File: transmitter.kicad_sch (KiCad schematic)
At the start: 0 parts

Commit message: Polished IO schematics
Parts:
- added U37: STM32H723ZGTx, Package_QFP:LQFP-144_20x20mm_P0.5mm, symbol MCU_ST_STM32H7:STM32H723ZGTx
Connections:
- new net: U37.107 (VSS), U37.120 (VSS), U37.130 (VSS), U37.16 (VSS), U37.38 (VSS), U37.51 (VSS), U37.61 (VSS), U37.83 (VSS), U37.94 (VSS)
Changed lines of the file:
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@@
 (kicad_sch (version 20230121) (generator eeschema)
-  (paper "A4")
-)
+  (paper "A4" portrait)

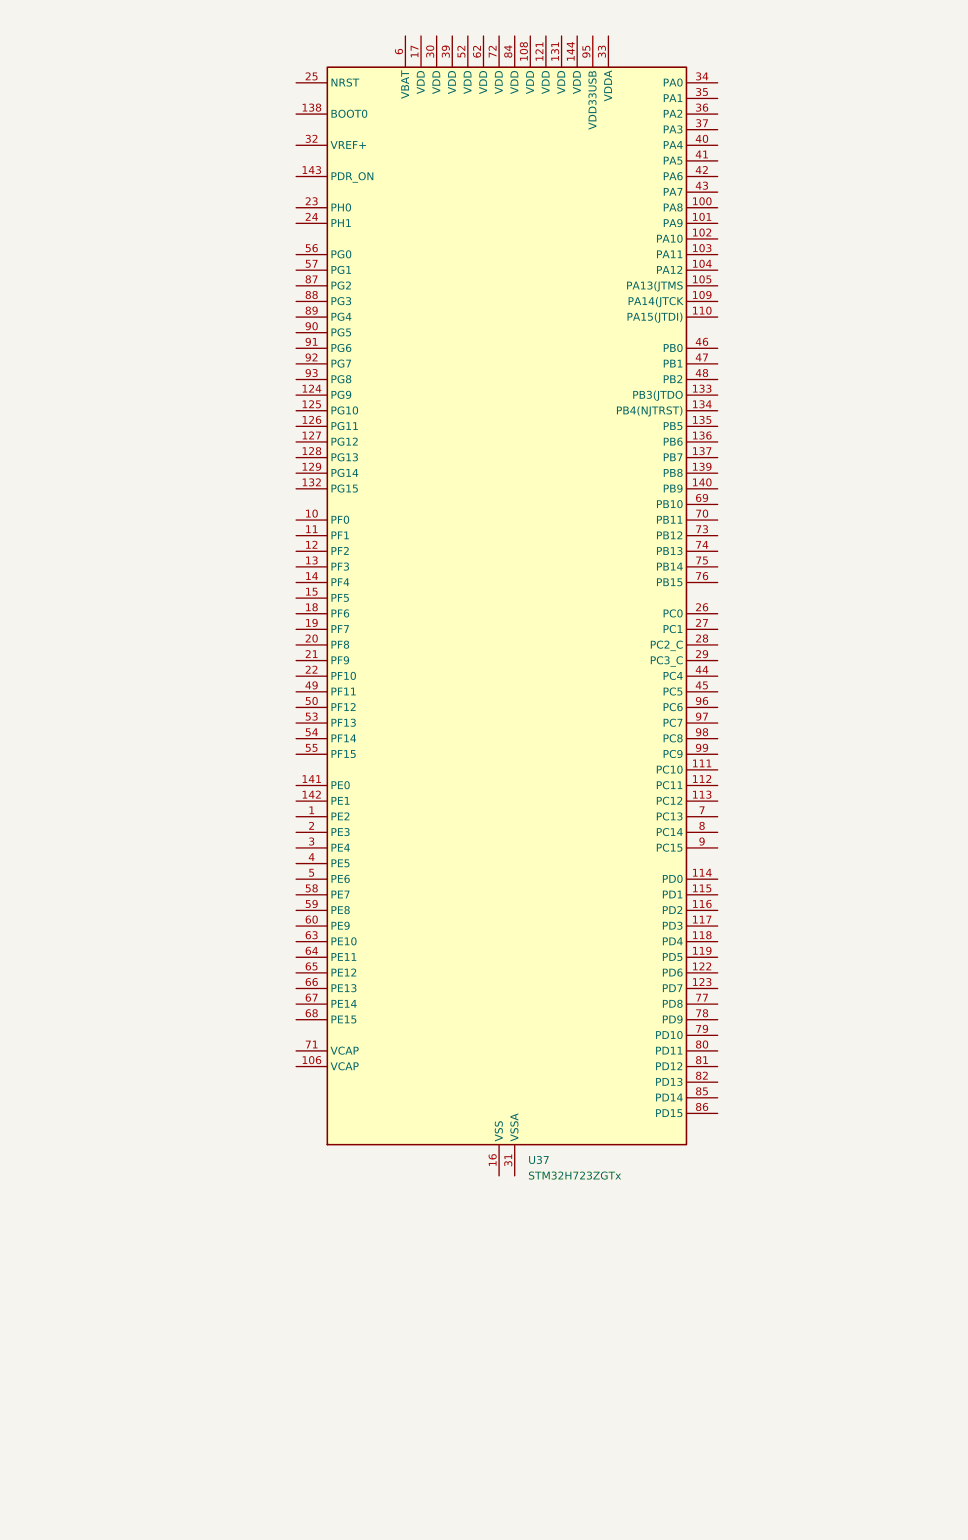
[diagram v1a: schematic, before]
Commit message: Set power routing for stm32
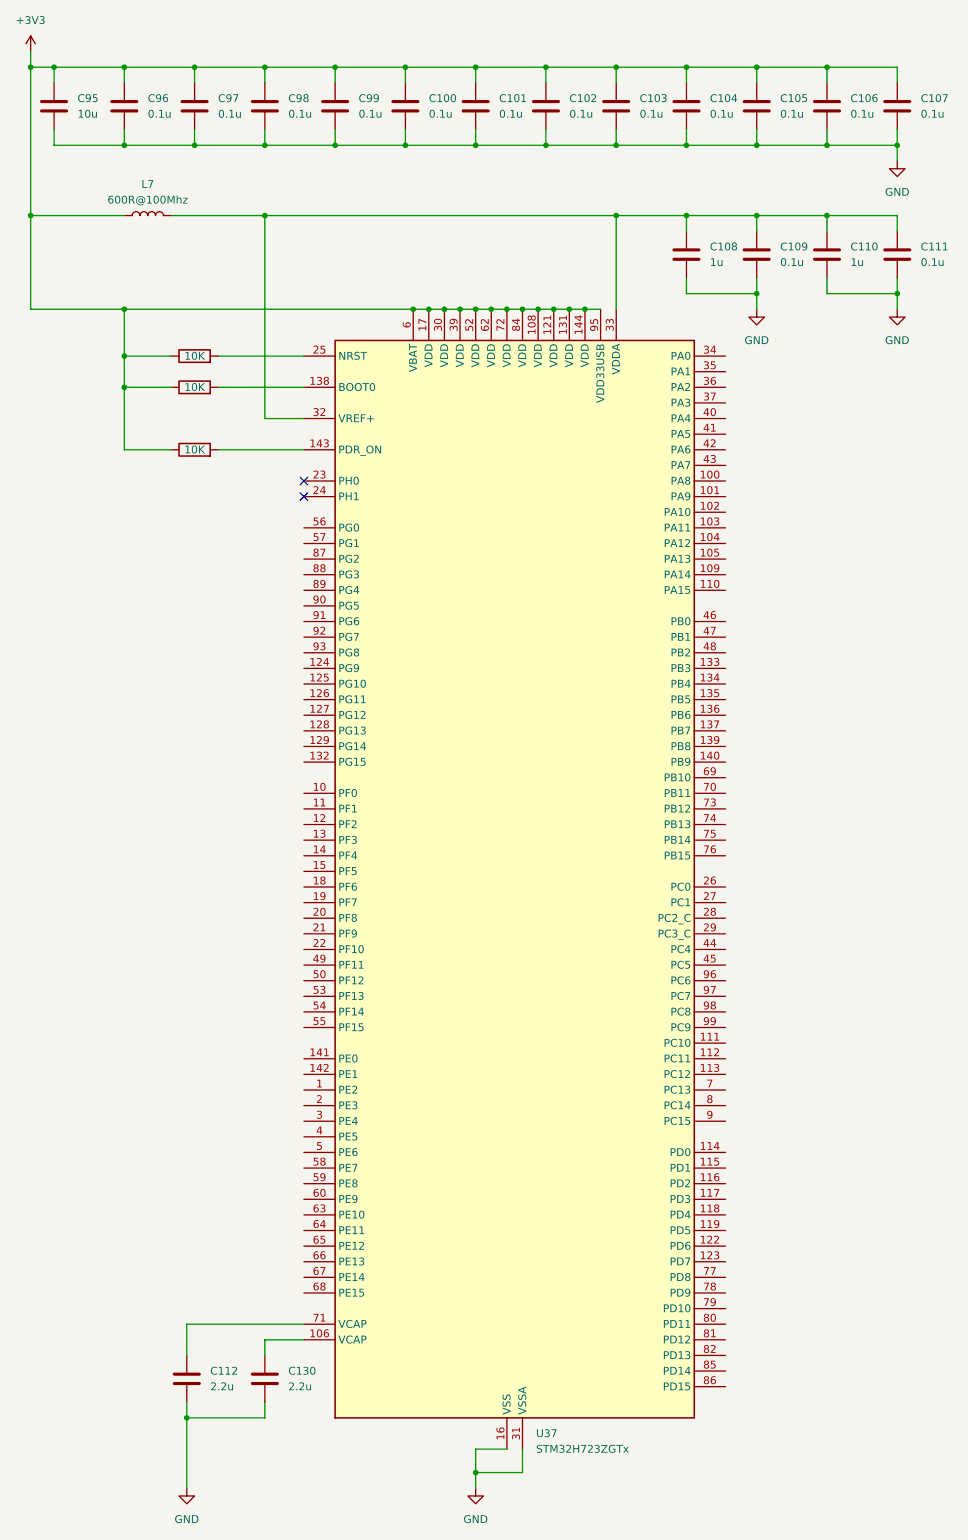
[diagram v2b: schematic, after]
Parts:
- added C100, C101, C102, C103, C104, C105, C106, C107, C109, C111, C96, C97, C98, C99: 0.1u, symbol Device:C
- added C108, C110: 1u, symbol Device:C
- added C112, C130: 2.2u, symbol Device:C
- added C95: 10u, symbol Device:C
- added L7: 600R@100Mhz, symbol Device:L
- added R187, R188, R189: 10K, symbol Device:R
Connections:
- net at U37.106 (VCAP): now also C130.1
- net GND: now reaches U37.107 (VSS), U37.120 (VSS), U37.130 (VSS), U37.16 (VSS), U37.38 (VSS), U37.51 (VSS), U37.61 (VSS), U37.83 (VSS), U37.94 (VSS)
- net GND: now also U37.31 (VSSA), C100.2, C101.2, C102.2, C103.2, C104.2, C105.2, C106.2, C107.2, C108.2, C109.2, C110.2, C111.2, C112.2, C130.2, C95.2, C96.2, C97.2, C98.2, C99.2
- net +3V3: now reaches U37.108 (VDD)
- net +3V3: now also U37.121 (VDD), U37.131 (VDD), U37.144 (VDD), U37.17 (VDD), U37.30 (VDD), U37.39 (VDD), U37.52 (VDD), U37.6 (VBAT), U37.62 (VDD), U37.72 (VDD), U37.84 (VDD), U37.95 (VDD33USB), C100.1, C101.1, C102.1, C103.1, C104.1, C105.1, C106.1, C107.1, C95.1, C96.1, C97.1, C98.1, C99.1, L7.1, R187.1, R188.1, R189.1
- net at U37.138 (BOOT0): now also R188.2
- net at U37.143 (PDR_ON): now also R189.2
- net at U37.25 (NRST): now also R187.2
- net at U37.32 (VREF+): now also U37.33 (VDDA), C108.1, C109.1, C110.1, C111.1, L7.2
- net at U37.71 (VCAP): now also C112.1
- no-connect marks 0 -> 2

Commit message: Assigned proper footprints for all components
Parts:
- removed C110: 1u, symbol Device:C
- removed C111: 0.1u, symbol Device:C
- C100, C101, C102, C103, C104, C105, C106, C107, C109, C96, C97, C98, C99: value 0.1u -> 100n; footprint (none) -> Capacitor_SMD:C_0603_1608Metric_Pad1.08x0.95mm_HandSolder
- C108, C112, C130: footprint (none) -> Capacitor_SMD:C_0805_2012Metric_Pad1.18x1.45mm_HandSolder
- C95: footprint (none) -> Capacitor_SMD:C_1206_3216Metric_Pad1.33x1.80mm_HandSolder
- L7: footprint (none) -> Inductor_SMD:L_0603_1608Metric_Pad1.05x0.95mm_HandSolder
- R187, R188, R189: footprint (none) -> Resistor_SMD:R_0603_1608Metric_Pad0.98x0.95mm_HandSolder
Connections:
- net at C108.1, C109.1, L7.2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: no longer U37.32 (VREF+)
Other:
- moved on the sheet: L7

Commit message: Updated boards hierarchy
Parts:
- renumbered C112 to C110, C130 to C111, R187 to R197, R188 to R199, R189 to R201

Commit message: Finished annotation
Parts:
- renumbered C95 to C301, C96 to C302, C97 to C303, C98 to C304, C99 to C305, C100 to C306, C101 to C307, C102 to C308, C103 to C309, C104 to C310, C105 to C311, C106 to C312, C107 to C313, C108 to C314, C109 to C315, C110 to C316, C111 to C317, L7 to L301, R197 to R301, R199 to R302, R201 to R303, U37 to U301
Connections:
- net DIN1_6: now reaches U301.10 (PF0)
- net SWD_IO: now reaches U301.105 (PA13)
- net SWD_CLK: now reaches U301.109 (PA14)
- net DIN1_5: now reaches U301.11 (PF1)
- net DIN5_5: now reaches U301.110 (PA15)
- net DIN5_1: now reaches U301.111 (PC10)
- net DIN5_2: now reaches U301.112 (PC11)
- net DIN5_3: now reaches U301.114 (PD0)
- net DIN5_4: now reaches U301.115 (PD1)
- net DIN1_4: now reaches U301.12 (PF2)
- net DIN6_1: now reaches U301.125 (PG10)
- net DIN6_2: now reaches U301.126 (PG11)
- net DIN6_3: now reaches U301.127 (PG12)
- net DIN6_4: now reaches U301.128 (PG13)
- net DIN1_3: now reaches U301.13 (PF3)
- net DIN5_6: now reaches U301.133 (PB3)
- net DIN6_5: now reaches U301.134 (PB4)
- net DIN6_6: now reaches U301.135 (PB5)
- net DIN1_2: now reaches U301.14 (PF4)
- net DIN1_1: now reaches U301.15 (PF5)
- net AIN1_1: now reaches U301.19 (PF7)
- net AIN1_2: now reaches U301.20 (PF8)
- net AIN2_1: now reaches U301.21 (PF9)
- net AIN2_2: now reaches U301.22 (PF10)
- net AIN3_2: now reaches U301.26 (PC0)
- net ETH_MDC: now reaches U301.27 (PC1)
- net VREF: now reaches U301.32 (VREF+)
- net AIN3_1: now reaches U301.34 (PA0)
- net ETH_REFCLK: now reaches U301.35 (PA1)
- net ETH_MDIO: now reaches U301.36 (PA2)
- net AIN4_1: now reaches U301.37 (PA3)
- net AIN4_2: now reaches U301.40 (PA4)
- net GENOUT: now reaches U301.41 (PA5)
- net ETH_CRS: now reaches U301.43 (PA7)
- net ETH_RXD0: now reaches U301.44 (PC4)
- net ETH_RXD1: now reaches U301.45 (PC5)
- net AIN5_1: now reaches U301.46 (PB0)
- net AIN5_2: now reaches U301.47 (PB1)
- net AIN6_1: now reaches U301.53 (PF13)
- net AIN6_2: now reaches U301.54 (PF14)
- net DIN2_1: now reaches U301.59 (PE8)
- net DIN2_5: now reaches U301.60 (PE9)
- net DIN2_2: now reaches U301.63 (PE10)
- net DIN2_6: now reaches U301.64 (PE11)
- net DIN2_3: now reaches U301.65 (PE12)
- net DIN2_4: now reaches U301.66 (PE13)
- net ETH_NRST: now reaches U301.69 (PB10)
- net ETH_TXEN: now reaches U301.70 (PB11)
- net ETH_TXD0: now reaches U301.73 (PB12)
- net ETH_TXD1: now reaches U301.74 (PB13)
- net DIN3_1: now reaches U301.77 (PD8)
- net DIN3_2: now reaches U301.78 (PD9)
- net DIN3_3: now reaches U301.79 (PD10)
- net DIN3_4: now reaches U301.80 (PD11)
- net DIN3_5: now reaches U301.81 (PD12)
- net DIN3_6: now reaches U301.82 (PD13)
- net DIN4_1: now reaches U301.90 (PG5)
- net DIN4_2: now reaches U301.91 (PG6)
- net DIN4_3: now reaches U301.92 (PG7)
- net DIN4_4: now reaches U301.93 (PG8)
- net DIN4_5: now reaches U301.96 (PC6)
- net DIN4_6: now reaches U301.97 (PC7)
- no-connect marks 2 -> 52
